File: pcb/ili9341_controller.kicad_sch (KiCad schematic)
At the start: 58 parts, among them J1 USB_B_Micro, J2 RP_SWD_CONN, SW1 RP_RST_SW, SW2 RP_USB_BOOT_SW, U1 ICE40UP5K-SG48ITR, U2 LM3880, U3 LD1117S33TR_SOT223, U4 LD1117S12TR_SOT223, U5 LD1117S25TR_SOT223, U6 RP2040, U7 W25Q128JVS, Y1 12MHz

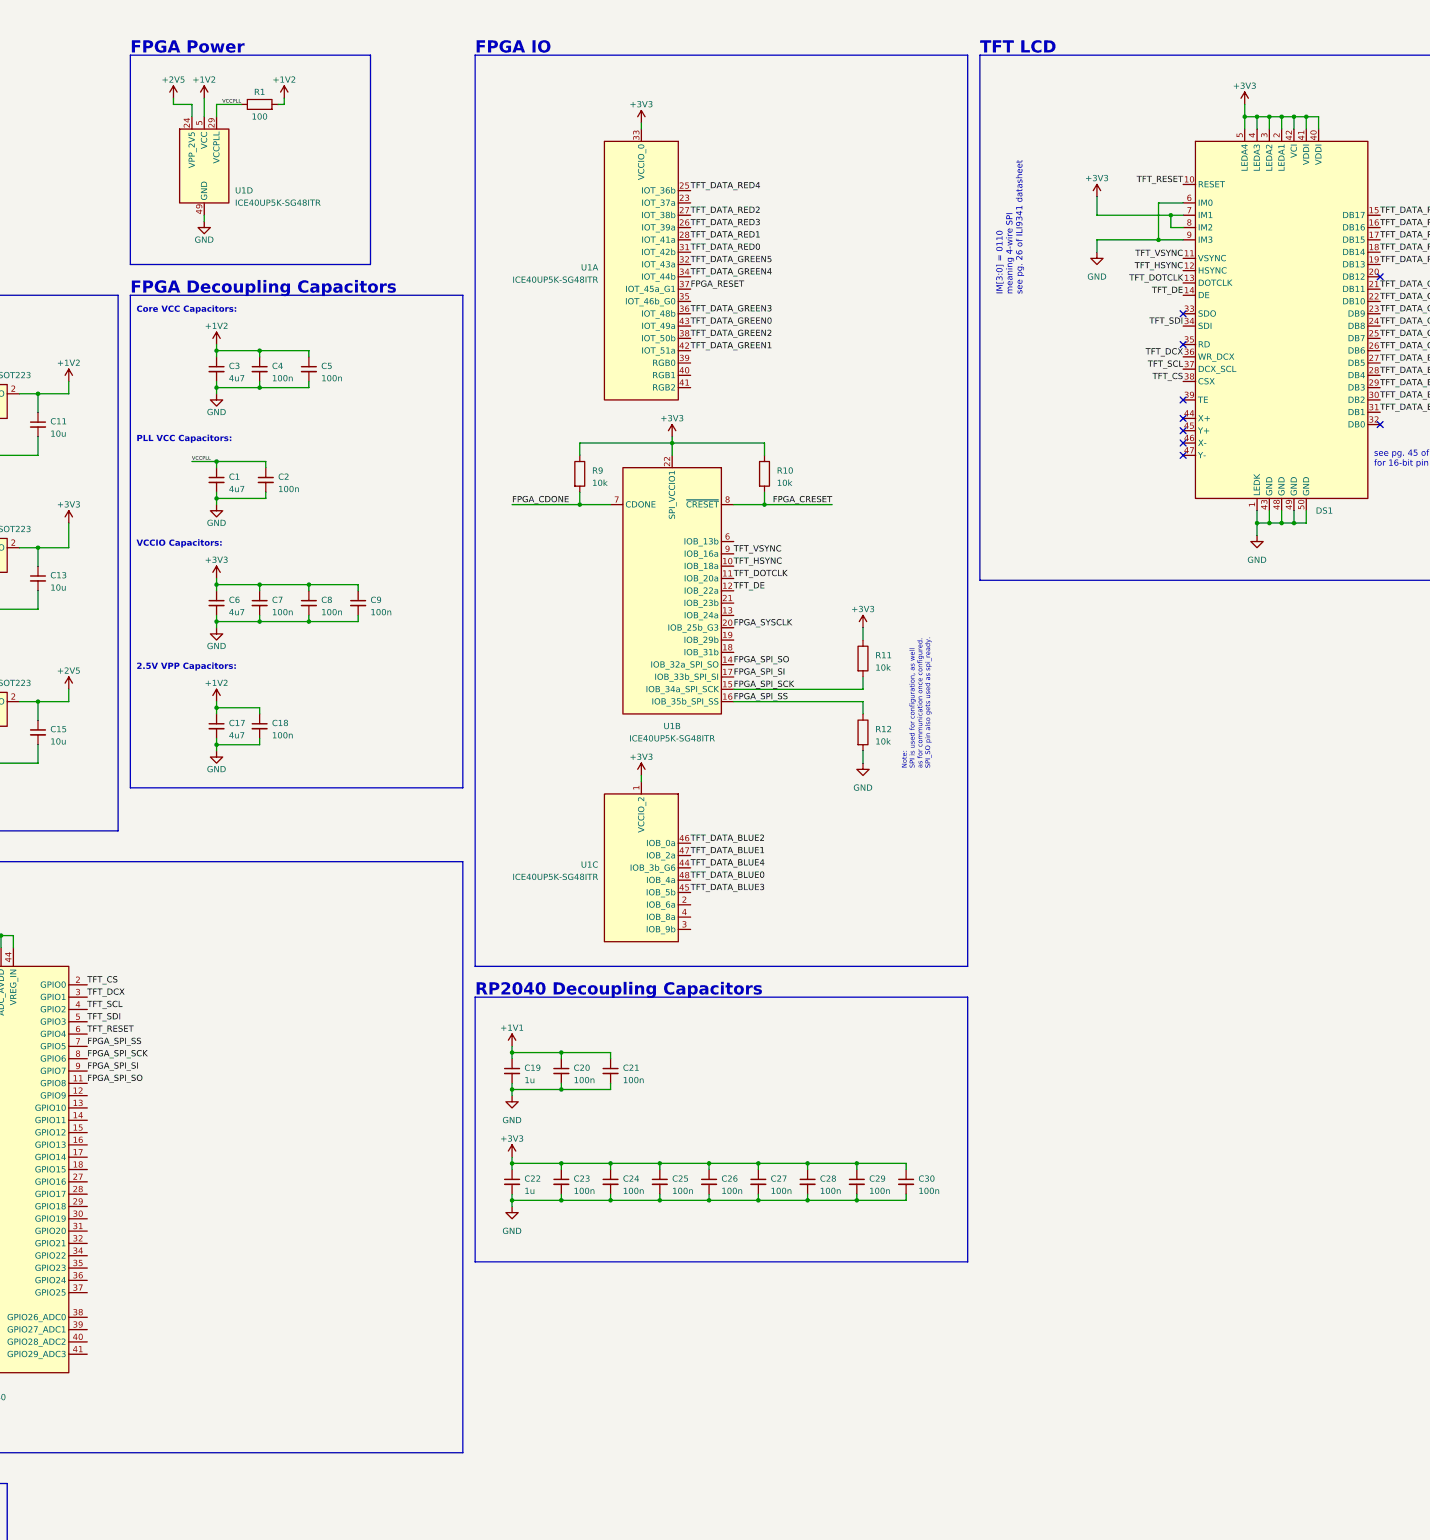
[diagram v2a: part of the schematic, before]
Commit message: add user-usable LEDs and power indicator LEDs
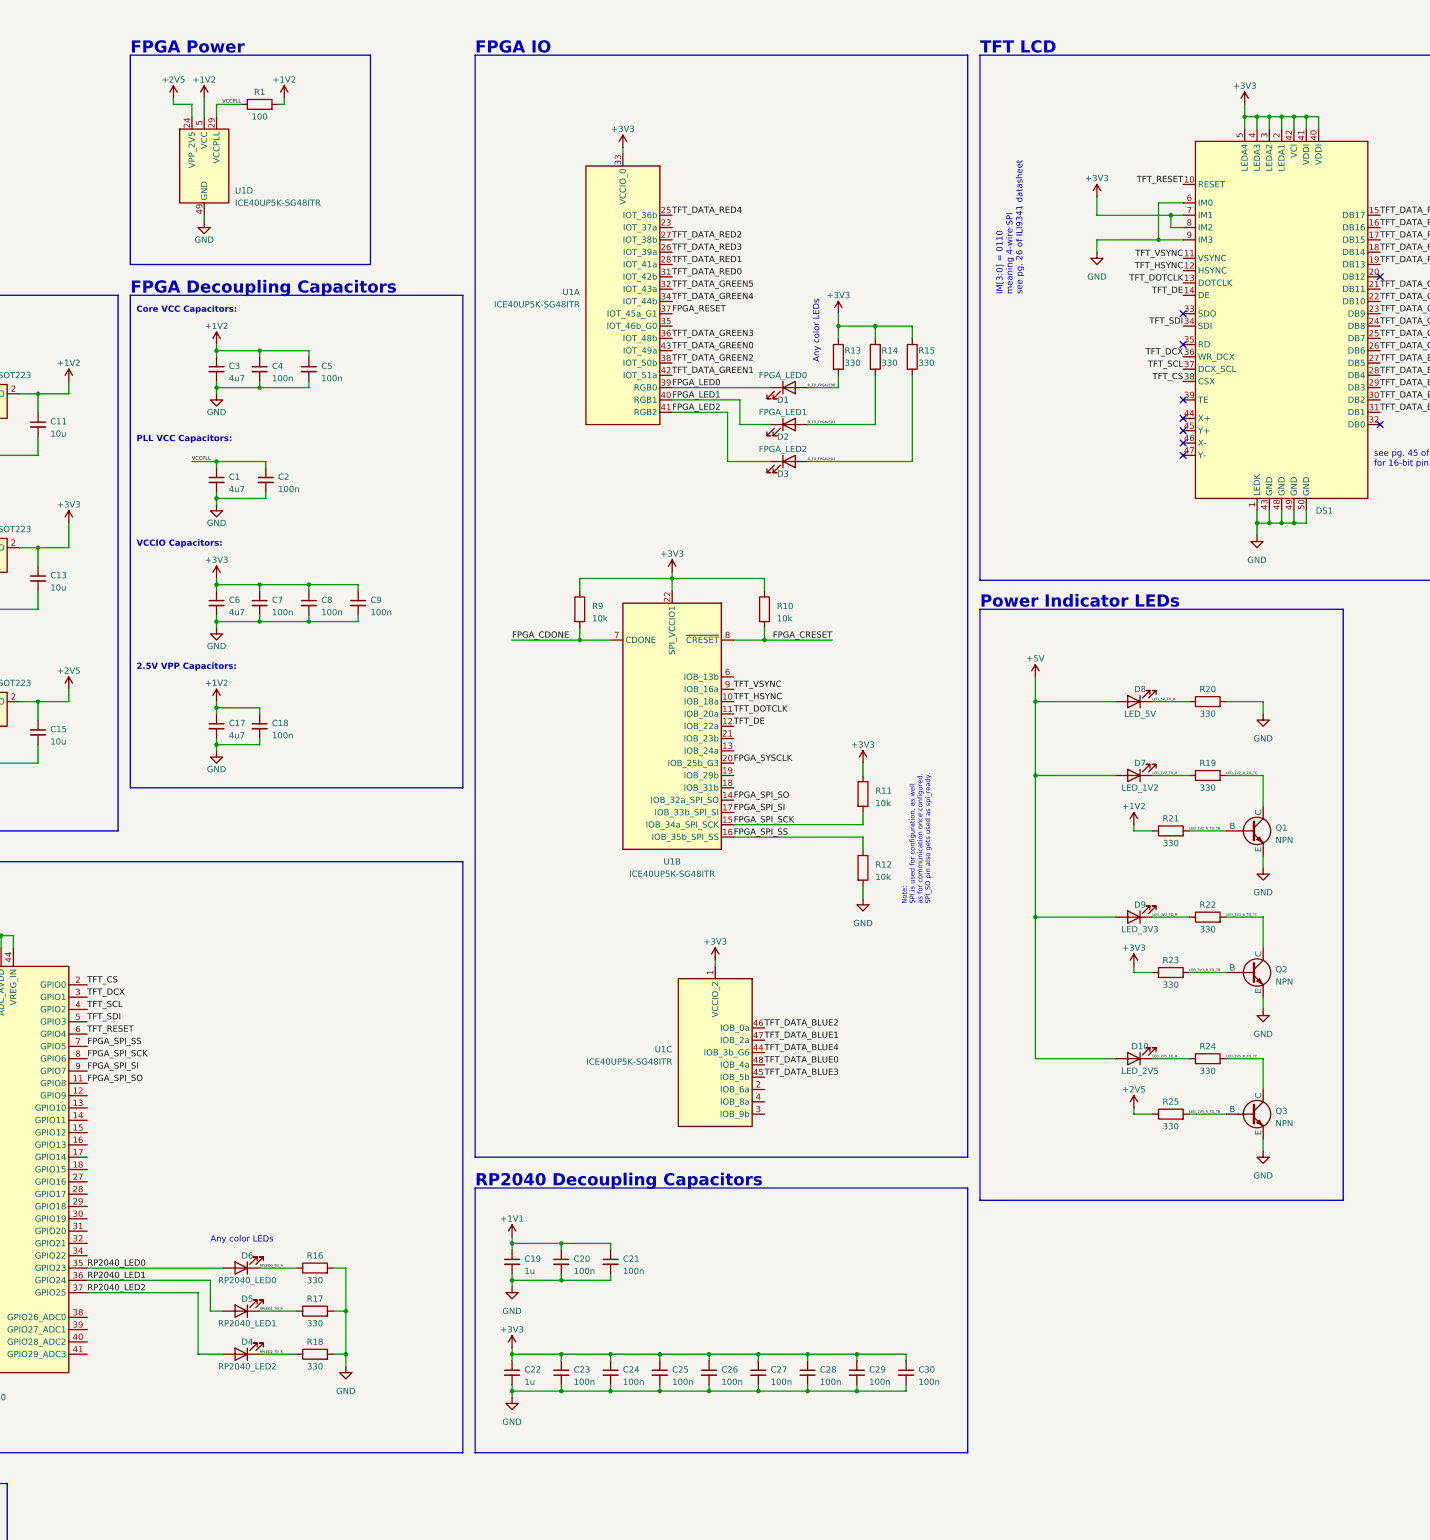
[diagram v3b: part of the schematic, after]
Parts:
- added D1: FPGA_LED0, symbol Device:LED
- added D10: LED_2V5, symbol Device:LED
- added D2: FPGA_LED1, symbol Device:LED
- added D3: FPGA_LED2, symbol Device:LED
- added D4: RP2040_LED2, symbol Device:LED
- added D5: RP2040_LED1, symbol Device:LED
- added D6: RP2040_LED0, symbol Device:LED
- added D7: LED_1V2, symbol Device:LED
- added D8: LED_5V, symbol Device:LED
- added D9: LED_3V3, symbol Device:LED
- added Q1, Q2, Q3: NPN, symbol Simulation_SPICE:NPN
- added R13, R14, R15, R16, R17, R18, R19, R20, R21, R22, R23, R24, R25: 330, symbol Device:R
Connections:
- net +1V2: now also R21.1
- net +2V5: now also R25.1
- net +3V3: now also R13.1, R14.1, R15.1, R23.1
- net +5V: now also D10.2 (A), D7.2 (A), D8.2 (A), D9.2 (A)
- net GND: now also Q1.3 (E), Q2.3 (E), Q3.3 (E), R16.2, R17.2, R18.2, R20.2
- net RP2040_LED0: now reaches U6.35 (GPIO23)
- net RP2040_LED0: now also D6.2 (A)
- net RP2040_LED1: now reaches U6.36 (GPIO24)
- net RP2040_LED1: now also D5.2 (A)
- net RP2040_LED2: now reaches U6.37 (GPIO25)
- net RP2040_LED2: now also D4.2 (A)
- net FPGA_LED0: now reaches U1.39 (RGB0)
- net FPGA_LED0: now also D1.1 (K)
- net FPGA_LED1: now reaches U1.40 (RGB1)
- net FPGA_LED1: now also D2.1 (K)
- net FPGA_LED2: now reaches U1.41 (RGB2)
- net FPGA_LED2: now also D3.1 (K)
- new net LED_1V2_R_TO_TB: Q1.2 (B), R21.2
- new net LED_1V2_R_TO_TC: Q1.1 (C), R19.2
- new net LED_1V2_TO_R: D7.1 (K), R19.1
- new net LED_2V5_R_TO_TB: Q3.2 (B), R25.2
- new net LED_2V5_R_TO_TC: Q3.1 (C), R24.2
- new net LED_2V5_TO_R: D10.1 (K), R24.1
- new net LED_3V3_R_TO_TB: Q2.2 (B), R23.2
- new net LED_3V3_R_TO_TC: Q2.1 (C), R22.2
- new net LED_3V3_TO_R: D9.1 (K), R22.1
- new net LED_5V_TO_R: D8.1 (K), R20.1
- new net RPLED0_TO_R: D6.1 (K), R16.1
- new net RPLED1_TO_R: D5.1 (K), R17.1
- new net RPLED2_TO_R: D4.1 (K), R18.1
- new net R_TO_FPGALED0: D1.2 (A), R13.2
- new net R_TO_FPGALED1: D2.2 (A), R14.2
- new net R_TO_FPGALED2: D3.2 (A), R15.2
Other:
- note added: "Any color LEDs"
- note added: "Power Indicator LEDs"
- moved on the sheet: C19, C20, C21, C22, C23, C24, C25, C26, C27, C28, C29, C30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
